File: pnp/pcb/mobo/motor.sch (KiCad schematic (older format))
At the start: 8 parts, among them M1 Stepper_Motor

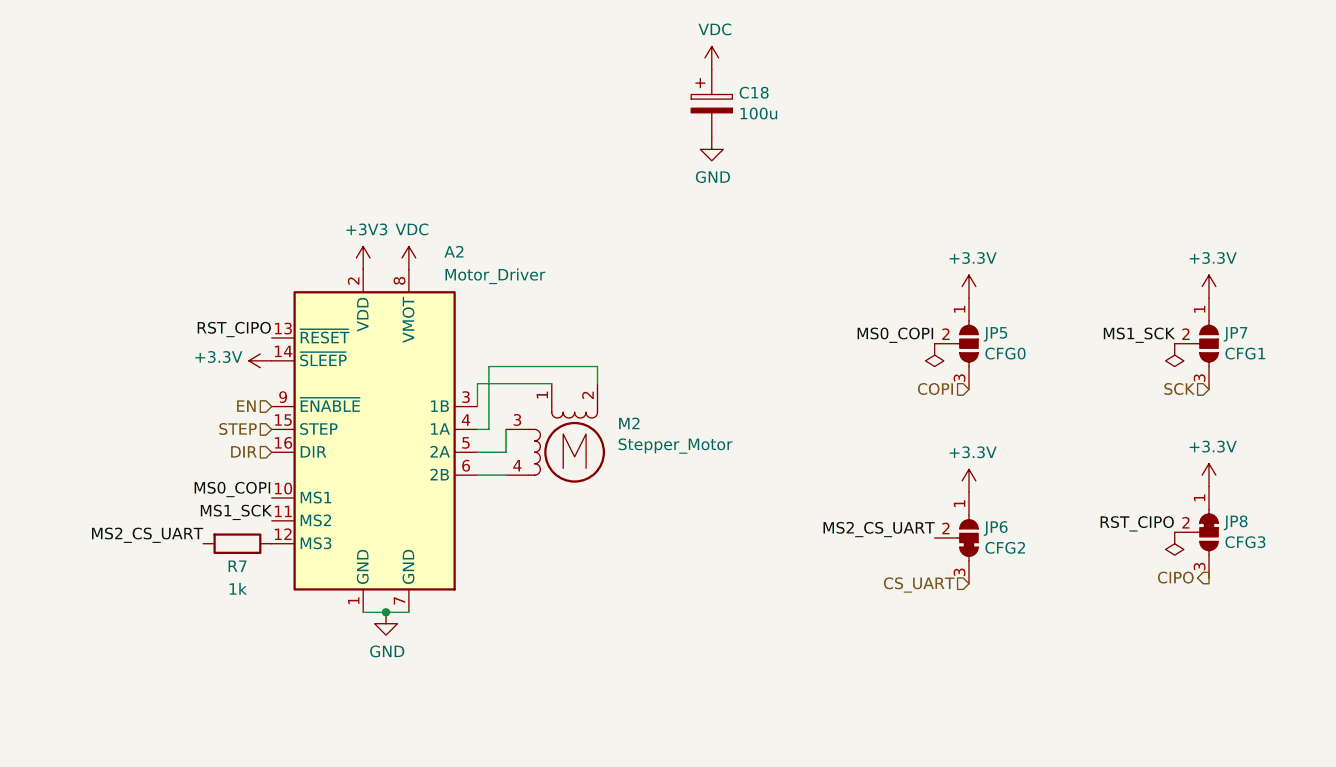
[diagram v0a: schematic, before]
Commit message: Fix DNP
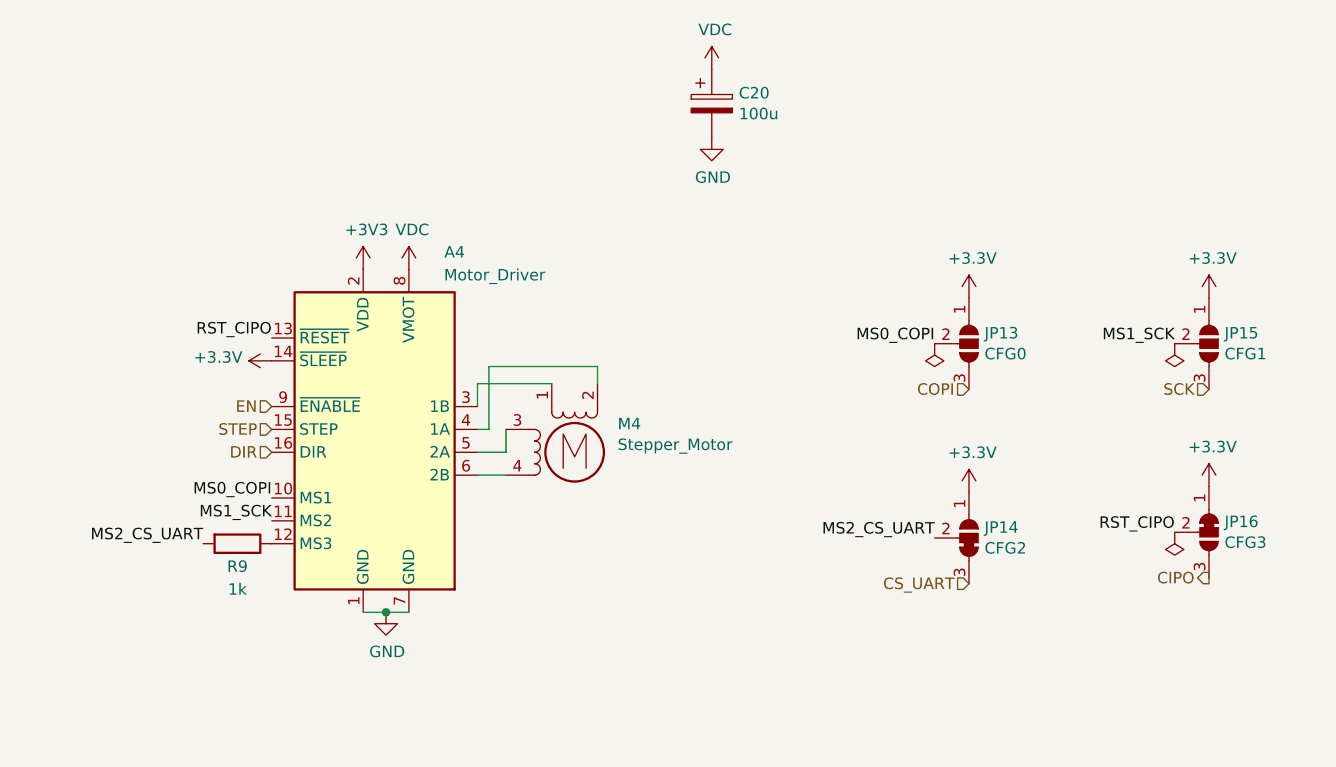
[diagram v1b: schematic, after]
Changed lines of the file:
@@
 AR Path="/5EB0C248/6035AFD9/602B8E60" Ref="A?"  Part="1"
 AR Path="/5EB0C248/6036900B/602B8E60" Ref="A?"  Part="1"
-F 0 "A2" H 4925 4525 50  0000 C CNN
+F 0 "A4" H 4925 4525 50  0000 C CNN
 F 1 "Motor_Driver" H 5100 4425 50  0000 C CNN
 F 2 "Module:Pololu_Breakout-16_15.2x20.3mm" H 4800 3000 50  0001 L CNN
@@
 AR Path="/5EB0C248/6035AFD9/602B8E66" Ref="#PWR?"  Part="1"
 AR Path="/5EB0C248/6036900B/602B8E66" Ref="#PWR?"  Part="1"
-F 0 "#PWR035" H 4625 4300 50  0001 C CNN
+F 0 "#PWR055" H 4625 4300 50  0001 C CNN
 F 1 "GND" H 4630 4377 50  0000 C CNN
 F 2 "" H 4625 4550 50  0001 C CNN
@@
 AR Path="/5EB0C248/6035AFD9/602B8E72" Ref="M?"  Part="1"
 AR Path="/5EB0C248/6036900B/602B8E72" Ref="M?"  Part="1"
-F 0 "M2" H 5638 3974 50  0000 L CNN
+F 0 "M4" H 5638 3974 50  0000 L CNN
 F 1 "Stepper_Motor" H 5638 3883 50  0000 L CNN
 F 2 "Connector_JST:JST_XH_B4B-XH-A_1x04_P2.50mm_Vertical" H 5460 3840 50  0001 C CNN
@@
 AR Path="/5EB0C248/6035AFD9/602B8E81" Ref="#PWR?"  Part="1"
 AR Path="/5EB0C248/6036900B/602B8E81" Ref="#PWR?"  Part="1"
-F 0 "#PWR034" H 4525 2900 50  0001 C CNN
+F 0 "#PWR054" H 4525 2900 50  0001 C CNN
 F 1 "+3V3" H 4540 3223 50  0000 C CNN
 F 2 "" H 4525 3050 50  0001 C CNN
@@
 AR Path="/5EB0C248/6035AFD9/602B8E8D" Ref="#PWR?"  Part="1"
 AR Path="/5EB0C248/6036900B/602B8E8D" Ref="#PWR?"  Part="1"
-F 0 "#PWR033" H 4125 3300 50  0001 C CNN
+F 0 "#PWR053" H 4125 3300 50  0001 C CNN
 F 1 "+3.3V" V 4140 3578 50  0000 L CNN
 F 2 "" H 4125 3450 50  0001 C CNN
@@
 AR Path="/5EB0C248/6035AFD9/602D9729" Ref="#PWR?"  Part="1"
 AR Path="/5EB0C248/6036900B/602D9729" Ref="#PWR?"  Part="1"
-F 0 "#PWR042" H 8225 3850 50  0001 C CNN
+F 0 "#PWR062" H 8225 3850 50  0001 C CNN
 F 1 "+3.3V" H 8240 4173 50  0000 C CNN
 F 2 "" H 8225 4000 50  0001 C CNN
@@
 AR Path="/5EB0C248/6035AFD9/602D973A" Ref="#PWR?"  Part="1"
 AR Path="/5EB0C248/6036900B/602D973A" Ref="#PWR?"  Part="1"
-F 0 "#PWR039" H 7175 3025 50  0001 C CNN
+F 0 "#PWR059" H 7175 3025 50  0001 C CNN
 F 1 "+3.3V" H 7190 3348 50  0000 C CNN
 F 2 "" H 7175 3175 50  0001 C CNN
@@
 AR Path="/5EB0C248/6035AFD9/602D9740" Ref="#PWR?"  Part="1"
 AR Path="/5EB0C248/6036900B/602D9740" Ref="#PWR?"  Part="1"
-F 0 "#PWR041" H 8225 3025 50  0001 C CNN
+F 0 "#PWR061" H 8225 3025 50  0001 C CNN
 F 1 "+3.3V" H 8240 3348 50  0000 C CNN
 F 2 "" H 8225 3175 50  0001 C CNN
@@
 AR Path="/5EB0C248/6035AFD9/602D9748" Ref="#PWR?"  Part="1"
 AR Path="/5EB0C248/6036900B/602D9748" Ref="#PWR?"  Part="1"
-F 0 "#PWR040" H 7175 3875 50  0001 C CNN
+F 0 "#PWR060" H 7175 3875 50  0001 C CNN
 F 1 "+3.3V" H 7190 4198 50  0000 C CNN
 F 2 "" H 7175 4025 50  0001 C CNN
@@
 AR Path="/5EB0C248/6035AFD9/603E21CF" Ref="#PWR?"  Part="1"
 AR Path="/5EB0C248/6036900B/603E21CF" Ref="#PWR?"  Part="1"
-F 0 "#PWR036" H 4725 2950 50  0001 C CNN
+F 0 "#PWR056" H 4725 2950 50  0001 C CNN
 F 1 "VDC" H 4740 3223 50  0000 C CNN
 F 2 "" H 4725 3050 50  0001 C CNN
@@
 AR Path="/5EB0C248/6035AFD9/604212D2" Ref="#PWR?"  Part="1"
 AR Path="/5EB0C248/6036900B/604212D2" Ref="#PWR?"  Part="1"
-F 0 "#PWR037" H 6050 2075 50  0001 C CNN
+F 0 "#PWR057" H 6050 2075 50  0001 C CNN
 F 1 "VDC" H 6065 2348 50  0000 C CNN
 F 2 "" H 6050 2175 50  0001 C CNN
@@
 AR Path="/5EB0C248/6035AFD9/604212D8" Ref="#PWR?"  Part="1"
 AR Path="/5EB0C248/6036900B/604212D8" Ref="#PWR?"  Part="1"
-F 0 "#PWR038" H 6050 2225 50  0001 C CNN
+F 0 "#PWR058" H 6050 2225 50  0001 C CNN
 F 1 "GND" H 6055 2302 50  0000 C CNN
 F 2 "" H 6050 2475 50  0001 C CNN
@@
 AR Path="/5EB0C248/6035AFD9/6040EB12" Ref="#FLG?"  Part="1"
 AR Path="/5EB0C248/6036900B/6040EB12" Ref="#FLG?"  Part="1"
-F 0 "#FLG09" H 8075 4275 50  0001 C CNN
+F 0 "#FLG015" H 8075 4275 50  0001 C CNN
 F 1 "PWR_FLAG" H 8075 4373 50  0001 C CNN
 F 2 "" H 8075 4200 50  0001 C CNN
@@
 AR Path="/5EB0C248/6035AFD9/6040EE3D" Ref="#FLG?"  Part="1"
 AR Path="/5EB0C248/6036900B/6040EE3D" Ref="#FLG?"  Part="1"
-F 0 "#FLG08" H 8075 3450 50  0001 C CNN
+F 0 "#FLG014" H 8075 3450 50  0001 C CNN
 F 1 "PWR_FLAG" H 8075 3548 50  0001 C CNN
 F 2 "" H 8075 3375 50  0001 C CNN
@@
 AR Path="/5EB0C248/6035AFD9/6040EFE9" Ref="#FLG?"  Part="1"
 AR Path="/5EB0C248/6036900B/6040EFE9" Ref="#FLG?"  Part="1"
-F 0 "#FLG07" H 7025 3450 50  0001 C CNN
+F 0 "#FLG013" H 7025 3450 50  0001 C CNN
 F 1 "PWR_FLAG" H 7025 3548 50  0001 C CNN
 F 2 "" H 7025 3375 50  0001 C CNN
@@
 AR Path="/5EB0C248/6035AFD9/604212CC" Ref="C?"  Part="1"
 AR Path="/5EB0C248/6036900B/604212CC" Ref="C?"  Part="1"
-F 0 "C18" H 6168 2371 50  0000 L CNN
+F 0 "C20" H 6168 2371 50  0000 L CNN
 F 1 "100u" H 6168 2280 50  0000 L CNN
 F 2 "Capacitor_SMD:CP_Elec_6.3x7.7" H 6088 2175 50  0001 C CNN
@@
 AR Path="/5EB0C248/6035AFD9/602B8E5A" Ref="R?"  Part="1"
 AR Path="/5EB0C248/6036900B/602B8E5A" Ref="R?"  Part="1"
-F 0 "R7" V 4075 4250 50  0000 C CNN
+F 0 "R9" V 4075 4250 50  0000 C CNN
 F 1 "1k" V 4175 4250 50  0000 C CNN
 F 2 "Resistor_SMD:R_0805_2012Metric" V 3905 4250 50  0001 C CNN
@@
 AR Path="/5EB0C248/6034863B/60728F27" Ref="JP12"  Part="1"
 AR Path="/5EB0C248/60348EA3/60728F27" Ref="JP16"  Part="1"
-F 0 "JP8" V 8179 4268 50  0000 L CNN
+F 0 "JP16" V 8179 4268 50  0000 L CNN
 F 1 "CFG3" V 8270 4268 50  0000 L CNN
 F 2 "Jumper:SolderJumper-3_P1.3mm_Bridged12_RoundedPad1.0x1.5mm" H 8225 4200 50  0001 C CNN
@@
 AR Path="/5EB0C248/6034863B/607348CB" Ref="JP11"  Part="1"
 AR Path="/5EB0C248/60348EA3/607348CB" Ref="JP15"  Part="1"
-F 0 "JP7" V 8179 3443 50  0000 L CNN
+F 0 "JP15" V 8179 3443 50  0000 L CNN
 F 1 "CFG1" V 8270 3443 50  0000 L CNN
 F 2 "Jumper:SolderJumper-3_P1.3mm_Open_RoundedPad1.0x1.5mm" H 8225 3375 50  0001 C CNN
@@
 AR Path="/5EB0C248/6034863B/6072716D" Ref="JP9"  Part="1"
 AR Path="/5EB0C248/60348EA3/6072716D" Ref="JP13"  Part="1"
-F 0 "JP5" V 7129 3443 50  0000 L CNN
+F 0 "JP13" V 7129 3443 50  0000 L CNN
 F 1 "CFG0" V 7220 3443 50  0000 L CNN
 F 2 "Jumper:SolderJumper-3_P1.3mm_Open_RoundedPad1.0x1.5mm" H 7175 3375 50  0001 C CNN
@@
 AR Path="/5EB0C248/6034863B/6105F3B4" Ref="JP10"  Part="1"
 AR Path="/5EB0C248/60348EA3/6105F3B4" Ref="JP14"  Part="1"
-F 0 "JP6" V 7221 4293 50  0000 L CNN
+F 0 "JP14" V 7221 4293 50  0000 L CNN
 F 1 "CFG2" V 7130 4293 50  0000 L CNN
 F 2 "index:SolderJumper-3_P1.3mm_Bridged23_RoundedPad1.0x1.5mm" H 7175 4225 50  0001 C CNN

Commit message: added testpoints for host usb port
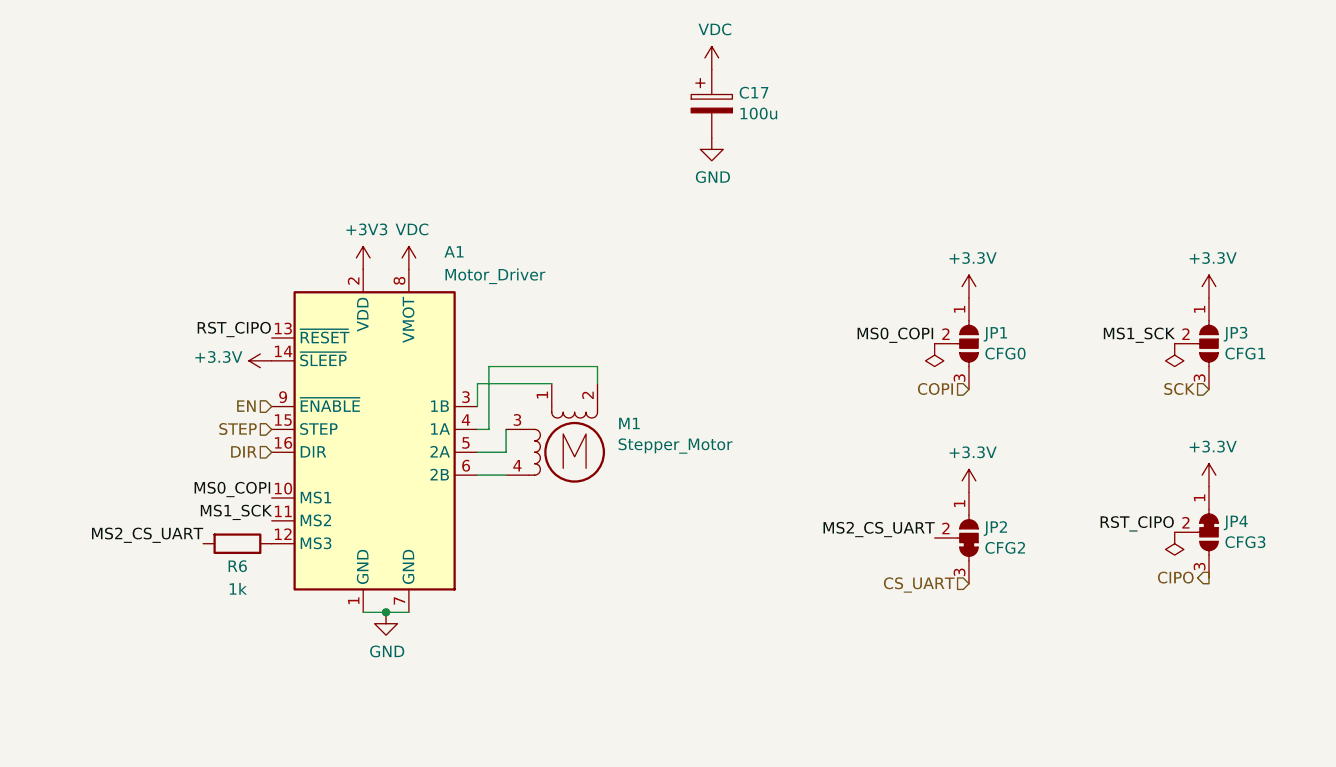
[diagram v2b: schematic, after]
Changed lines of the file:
@@
 $Descr A4 11693 8268
 encoding utf-8
-Sheet 4 16
+Sheet 3 16
 Title "Motor"
 Date "2021-02-19"
@@
 AR Path="/5EB0C248/6035AFD9/602B8E60" Ref="A?"  Part="1"
 AR Path="/5EB0C248/6036900B/602B8E60" Ref="A?"  Part="1"
-F 0 "A4" H 4925 4525 50  0000 C CNN
+F 0 "A1" H 4925 4525 50  0000 C CNN
 F 1 "Motor_Driver" H 5100 4425 50  0000 C CNN
 F 2 "Module:Pololu_Breakout-16_15.2x20.3mm" H 4800 3000 50  0001 L CNN
@@
 AR Path="/5EB0C248/6035AFD9/602B8E66" Ref="#PWR?"  Part="1"
 AR Path="/5EB0C248/6036900B/602B8E66" Ref="#PWR?"  Part="1"
-F 0 "#PWR055" H 4625 4300 50  0001 C CNN
+F 0 "#PWR025" H 4625 4300 50  0001 C CNN
 F 1 "GND" H 4630 4377 50  0000 C CNN
 F 2 "" H 4625 4550 50  0001 C CNN
@@
 AR Path="/5EB0C248/6035AFD9/602B8E72" Ref="M?"  Part="1"
 AR Path="/5EB0C248/6036900B/602B8E72" Ref="M?"  Part="1"
-F 0 "M4" H 5638 3974 50  0000 L CNN
+F 0 "M1" H 5638 3974 50  0000 L CNN
 F 1 "Stepper_Motor" H 5638 3883 50  0000 L CNN
 F 2 "Connector_JST:JST_XH_B4B-XH-A_1x04_P2.50mm_Vertical" H 5460 3840 50  0001 C CNN
@@
 AR Path="/5EB0C248/6035AFD9/602B8E81" Ref="#PWR?"  Part="1"
 AR Path="/5EB0C248/6036900B/602B8E81" Ref="#PWR?"  Part="1"
-F 0 "#PWR054" H 4525 2900 50  0001 C CNN
+F 0 "#PWR024" H 4525 2900 50  0001 C CNN
 F 1 "+3V3" H 4540 3223 50  0000 C CNN
 F 2 "" H 4525 3050 50  0001 C CNN
@@
 AR Path="/5EB0C248/6035AFD9/602B8E8D" Ref="#PWR?"  Part="1"
 AR Path="/5EB0C248/6036900B/602B8E8D" Ref="#PWR?"  Part="1"
-F 0 "#PWR053" H 4125 3300 50  0001 C CNN
+F 0 "#PWR023" H 4125 3300 50  0001 C CNN
 F 1 "+3.3V" V 4140 3578 50  0000 L CNN
 F 2 "" H 4125 3450 50  0001 C CNN
@@
 AR Path="/5EB0C248/6035AFD9/602D9729" Ref="#PWR?"  Part="1"
 AR Path="/5EB0C248/6036900B/602D9729" Ref="#PWR?"  Part="1"
-F 0 "#PWR062" H 8225 3850 50  0001 C CNN
+F 0 "#PWR032" H 8225 3850 50  0001 C CNN
 F 1 "+3.3V" H 8240 4173 50  0000 C CNN
 F 2 "" H 8225 4000 50  0001 C CNN
@@
 AR Path="/5EB0C248/6035AFD9/602D973A" Ref="#PWR?"  Part="1"
 AR Path="/5EB0C248/6036900B/602D973A" Ref="#PWR?"  Part="1"
-F 0 "#PWR059" H 7175 3025 50  0001 C CNN
+F 0 "#PWR029" H 7175 3025 50  0001 C CNN
 F 1 "+3.3V" H 7190 3348 50  0000 C CNN
 F 2 "" H 7175 3175 50  0001 C CNN
@@
 AR Path="/5EB0C248/6035AFD9/602D9740" Ref="#PWR?"  Part="1"
 AR Path="/5EB0C248/6036900B/602D9740" Ref="#PWR?"  Part="1"
-F 0 "#PWR061" H 8225 3025 50  0001 C CNN
+F 0 "#PWR031" H 8225 3025 50  0001 C CNN
 F 1 "+3.3V" H 8240 3348 50  0000 C CNN
 F 2 "" H 8225 3175 50  0001 C CNN
@@
 AR Path="/5EB0C248/6035AFD9/602D9748" Ref="#PWR?"  Part="1"
 AR Path="/5EB0C248/6036900B/602D9748" Ref="#PWR?"  Part="1"
-F 0 "#PWR060" H 7175 3875 50  0001 C CNN
+F 0 "#PWR030" H 7175 3875 50  0001 C CNN
 F 1 "+3.3V" H 7190 4198 50  0000 C CNN
 F 2 "" H 7175 4025 50  0001 C CNN
@@
 AR Path="/5EB0C248/6035AFD9/603E21CF" Ref="#PWR?"  Part="1"
 AR Path="/5EB0C248/6036900B/603E21CF" Ref="#PWR?"  Part="1"
-F 0 "#PWR056" H 4725 2950 50  0001 C CNN
+F 0 "#PWR026" H 4725 2950 50  0001 C CNN
 F 1 "VDC" H 4740 3223 50  0000 C CNN
 F 2 "" H 4725 3050 50  0001 C CNN
@@
 AR Path="/5EB0C248/6035AFD9/604212D2" Ref="#PWR?"  Part="1"
 AR Path="/5EB0C248/6036900B/604212D2" Ref="#PWR?"  Part="1"
-F 0 "#PWR057" H 6050 2075 50  0001 C CNN
+F 0 "#PWR027" H 6050 2075 50  0001 C CNN
 F 1 "VDC" H 6065 2348 50  0000 C CNN
 F 2 "" H 6050 2175 50  0001 C CNN
@@
 AR Path="/5EB0C248/6035AFD9/604212D8" Ref="#PWR?"  Part="1"
 AR Path="/5EB0C248/6036900B/604212D8" Ref="#PWR?"  Part="1"
-F 0 "#PWR058" H 6050 2225 50  0001 C CNN
+F 0 "#PWR028" H 6050 2225 50  0001 C CNN
 F 1 "GND" H 6055 2302 50  0000 C CNN
 F 2 "" H 6050 2475 50  0001 C CNN
@@
 AR Path="/5EB0C248/6035AFD9/6040EB12" Ref="#FLG?"  Part="1"
 AR Path="/5EB0C248/6036900B/6040EB12" Ref="#FLG?"  Part="1"
-F 0 "#FLG015" H 8075 4275 50  0001 C CNN
+F 0 "#FLG06" H 8075 4275 50  0001 C CNN
 F 1 "PWR_FLAG" H 8075 4373 50  0001 C CNN
 F 2 "" H 8075 4200 50  0001 C CNN
@@
 AR Path="/5EB0C248/6035AFD9/6040EE3D" Ref="#FLG?"  Part="1"
 AR Path="/5EB0C248/6036900B/6040EE3D" Ref="#FLG?"  Part="1"
-F 0 "#FLG014" H 8075 3450 50  0001 C CNN
+F 0 "#FLG05" H 8075 3450 50  0001 C CNN
 F 1 "PWR_FLAG" H 8075 3548 50  0001 C CNN
 F 2 "" H 8075 3375 50  0001 C CNN
@@
 AR Path="/5EB0C248/6035AFD9/6040EFE9" Ref="#FLG?"  Part="1"
 AR Path="/5EB0C248/6036900B/6040EFE9" Ref="#FLG?"  Part="1"
-F 0 "#FLG013" H 7025 3450 50  0001 C CNN
+F 0 "#FLG04" H 7025 3450 50  0001 C CNN
 F 1 "PWR_FLAG" H 7025 3548 50  0001 C CNN
 F 2 "" H 7025 3375 50  0001 C CNN
@@
 AR Path="/5EB0C248/6035AFD9/604212CC" Ref="C?"  Part="1"
 AR Path="/5EB0C248/6036900B/604212CC" Ref="C?"  Part="1"
-F 0 "C20" H 6168 2371 50  0000 L CNN
+F 0 "C17" H 6168 2371 50  0000 L CNN
 F 1 "100u" H 6168 2280 50  0000 L CNN
 F 2 "Capacitor_SMD:CP_Elec_6.3x7.7" H 6088 2175 50  0001 C CNN
@@
 AR Path="/5EB0C248/6035AFD9/602B8E5A" Ref="R?"  Part="1"
 AR Path="/5EB0C248/6036900B/602B8E5A" Ref="R?"  Part="1"
-F 0 "R9" V 4075 4250 50  0000 C CNN
+F 0 "R6" V 4075 4250 50  0000 C CNN
 F 1 "1k" V 4175 4250 50  0000 C CNN
 F 2 "Resistor_SMD:R_0805_2012Metric" V 3905 4250 50  0001 C CNN
@@
 AR Path="/5EB0C248/6034863B/60728F27" Ref="JP12"  Part="1"
 AR Path="/5EB0C248/60348EA3/60728F27" Ref="JP16"  Part="1"
-F 0 "JP16" V 8179 4268 50  0000 L CNN
+F 0 "JP4" V 8179 4268 50  0000 L CNN
 F 1 "CFG3" V 8270 4268 50  0000 L CNN
 F 2 "Jumper:SolderJumper-3_P1.3mm_Bridged12_RoundedPad1.0x1.5mm" H 8225 4200 50  0001 C CNN
@@
 AR Path="/5EB0C248/6034863B/607348CB" Ref="JP11"  Part="1"
 AR Path="/5EB0C248/60348EA3/607348CB" Ref="JP15"  Part="1"
-F 0 "JP15" V 8179 3443 50  0000 L CNN
+F 0 "JP3" V 8179 3443 50  0000 L CNN
 F 1 "CFG1" V 8270 3443 50  0000 L CNN
 F 2 "Jumper:SolderJumper-3_P1.3mm_Open_RoundedPad1.0x1.5mm" H 8225 3375 50  0001 C CNN
@@
 AR Path="/5EB0C248/6034863B/6072716D" Ref="JP9"  Part="1"
 AR Path="/5EB0C248/60348EA3/6072716D" Ref="JP13"  Part="1"
-F 0 "JP13" V 7129 3443 50  0000 L CNN
+F 0 "JP1" V 7129 3443 50  0000 L CNN
 F 1 "CFG0" V 7220 3443 50  0000 L CNN
 F 2 "Jumper:SolderJumper-3_P1.3mm_Open_RoundedPad1.0x1.5mm" H 7175 3375 50  0001 C CNN
@@
 AR Path="/5EB0C248/6034863B/6105F3B4" Ref="JP10"  Part="1"
 AR Path="/5EB0C248/60348EA3/6105F3B4" Ref="JP14"  Part="1"
-F 0 "JP14" V 7221 4293 50  0000 L CNN
+F 0 "JP2" V 7221 4293 50  0000 L CNN
 F 1 "CFG2" V 7130 4293 50  0000 L CNN
 F 2 "index:SolderJumper-3_P1.3mm_Bridged23_RoundedPad1.0x1.5mm" H 7175 4225 50  0001 C CNN

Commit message: Schematic improvement proposal
Discord
@jessevdz

Fixes:
-Proper hierarchical structure
Label inside the sheets with their local name
Then connect them together at sheet-level.
- Split into functional blocks
Just like with software its good to have one function per group of components.
For example: the power input, reverse polarity protection, buckconverter, multiplexer and LDO
were connected as one block. Now they are split into their functional blocks.
- Used smaller symbols
Some symbols used their large variant, which looks a bit funny in normal schematics
For example some R's have been changed to R_Small's.
- Align symbols to grid
A lot of the symbols were off the default 50mil grid.

And a lot of other general fixes in readability and structure.
Electrically the schematic should be the same.
Improvements that would require a schematic change can possibly
be done later in a seperate commit.
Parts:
- removed M1: Stepper_Motor, Connector_JST:JST_XH_B4B-XH-A_1x04_P2.50mm_Vertical, symbol Motor:Stepper_Motor_bipolar
- added M?: Stepper_Motor, Connector_JST:JST_XH_B4B-XH-A_1x04_P2.50mm_Vertical, symbol Motor:Stepper_Motor_bipolar
- C17: symbol Device:CP -> Device:CP_Small
- JP6: symbol index:SolderJumper_3_Bridged23 -> mobo-rescue:SolderJumper_3_Bridged23-index
- R6: symbol Device:R -> Device:R_Small
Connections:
- net 1B: now reaches A1.3 (1B)
- net 1B: now also M?.1
- net 1A: now reaches A1.4 (1A)
- net 1A: now also M?.2 (-)
- net 2A: now reaches A1.5 (2A)
- net 2A: now also M?.3
- net 2B: now reaches A1.6 (2B)
- net 2B: now also M?.4
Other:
- note added: "Configuration jumpers"
- note added: "Driver"
- moved on the sheet: A2, C18, JP5, JP6, JP7, JP8, R7
